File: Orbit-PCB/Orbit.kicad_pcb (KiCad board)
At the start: 2 copper layers, 149.8 x 115.2 mm, 129 parts, among them J1 PJ-3200B-4A, J2 AVR-ISP-6, Q1 2N7002, SW1 SW_Push, U1 ATmega32U4-MU, U2 PRTR5V0U2X, Y1 16MHz

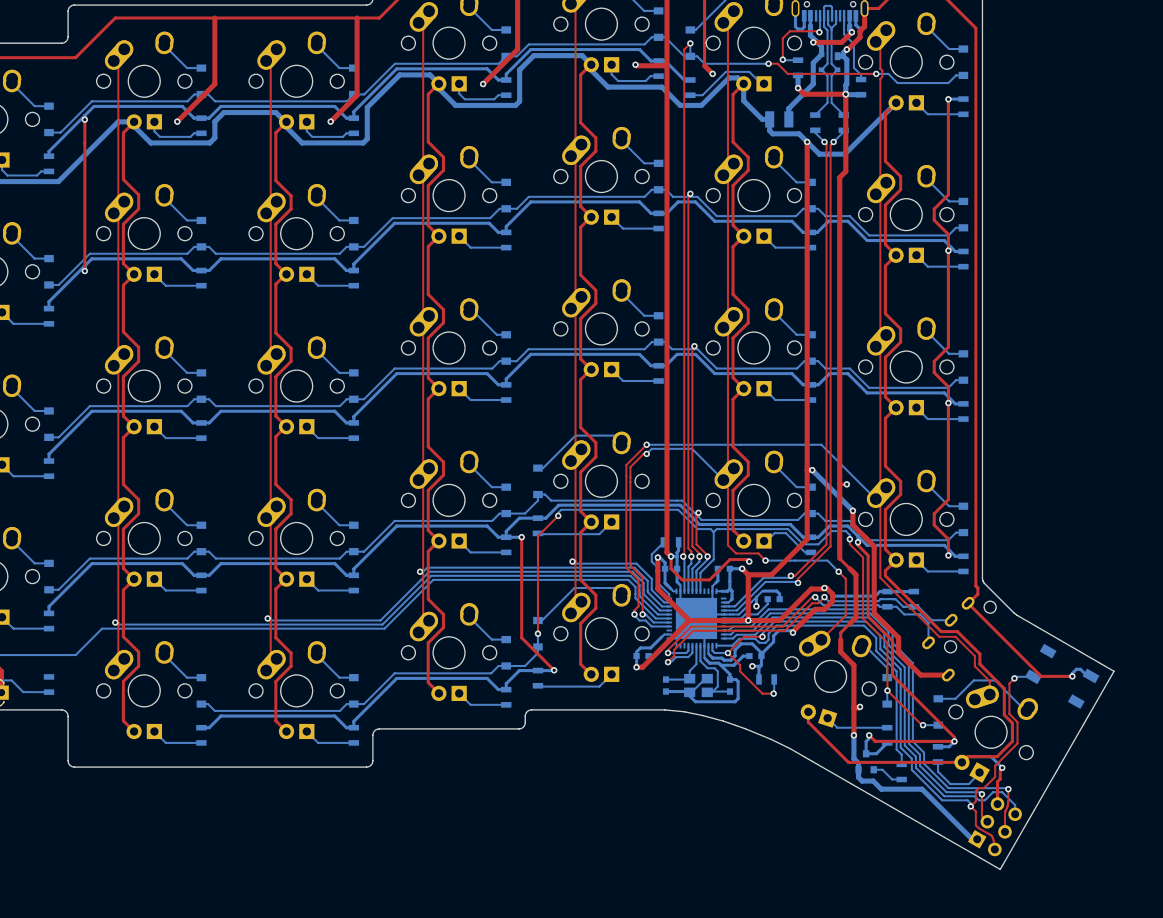
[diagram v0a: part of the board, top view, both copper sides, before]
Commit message: Round corner and route indicator LED
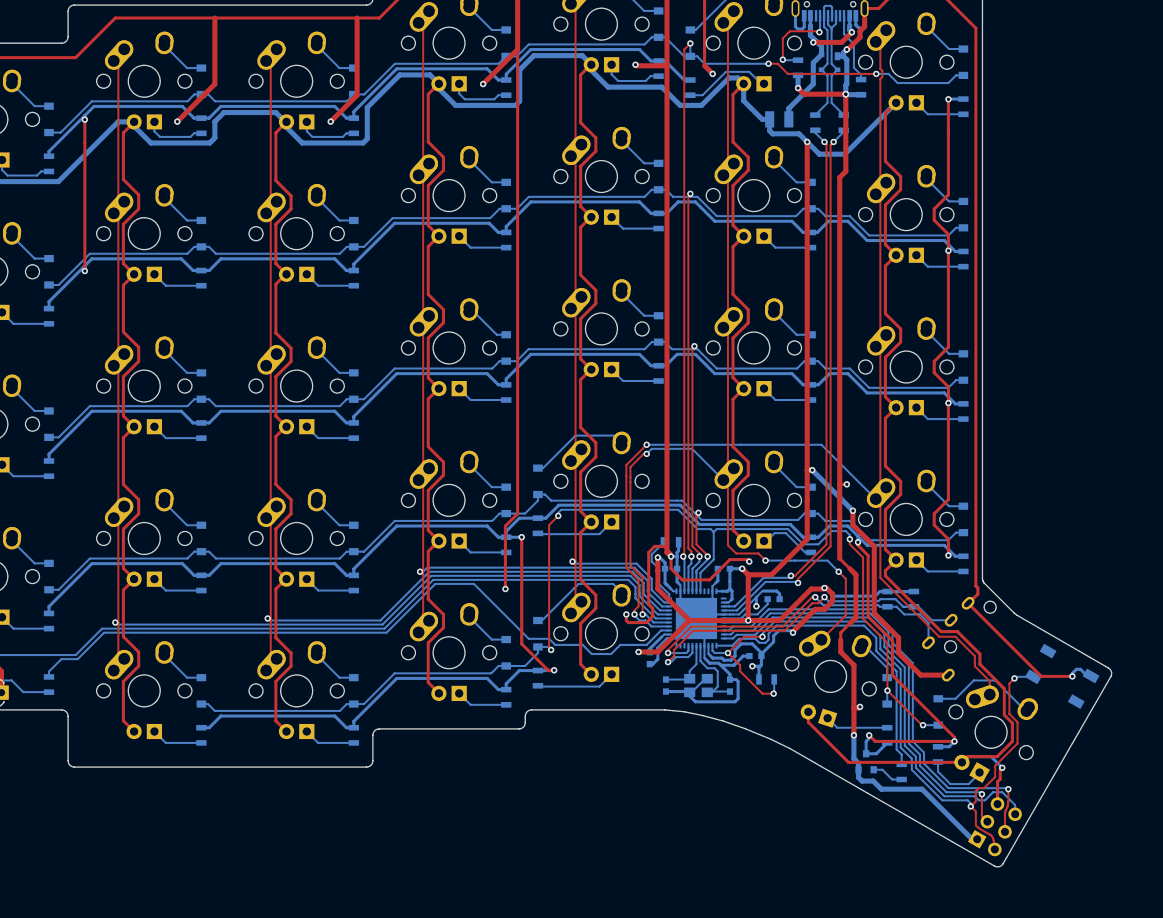
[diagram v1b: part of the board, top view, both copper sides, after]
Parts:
- moved C5 0.92 mm to (121.9, 117.3), turned to 270 degrees
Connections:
- U1 pad 25: Net-(U1-Pad25) -> LEDIND
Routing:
- net LEDIND: track 0.00 -> 87.6 mm
- net GND: track 678.0 -> 763.5 mm, vias 16 -> 18
- net +5V: track 969.3 -> 966.4 mm
- net ROW4: track 143.1 -> 144.8 mm
- net Net-(D32-Pad2): track 12.4 -> 13.4 mm
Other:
- board size 149.8 x 115.2 mm -> 149.5 x 114.9 mm
- net class POWER: trace_width 0.635 -> 0.381

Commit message: Both halves roughly complete, begin cleaning
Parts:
- added C10: 1uF, Capacitors_SMD:C_0603, B.Cu at (228.2, 116.1)
- added C11: 0.1uF, Capacitors_SMD:C_0603, B.Cu at (238.5, 122.5)
- added C12: 0.1uF, Capacitors_SMD:C_0603, B.Cu at (228.5, 110.6)
- added C13: 0.1uF, Capacitors_SMD:C_0603, B.Cu at (241.7, 112.1)
- added C14: 10uF, Capacitors_SMD:C_0603, B.Cu at (230.1, 120.7)
- added C8: 22pF, Capacitors_SMD:C_0603, B.Cu at (238.8, 108.0)
- added C9: 22pF, Capacitors_SMD:C_0603, B.Cu at (231.9, 108.0)
- added D36: SOD-123, Diodes_SMD:D_SOD-123, B.Cu at (204.0, 42.9)
- added D37: SOD-123, Diodes_SMD:D_SOD-123, B.Cu at (237.3, 40.5)
- added D38: SOD-123, Diodes_SMD:D_SOD-123, B.Cu at (256.4, 38.1)
- added D39: SOD-123, Diodes_SMD:D_SOD-123, B.Cu at (275.4, 40.5)
- added D40: SOD-123, Diodes_SMD:D_SOD-123, B.Cu at (294.5, 45.2)
- added D41: SOD-123, Diodes_SMD:D_SOD-123, B.Cu at (313.5, 45.2)
- added D42: SOD-123, Diodes_SMD:D_SOD-123, B.Cu at (332.6, 50.0)
- added D43: SOD-123, Diodes_SMD:D_SOD-123, B.Cu at (218.3, 61.9)
- added D44: SOD-123, Diodes_SMD:D_SOD-123, B.Cu at (237.3, 59.5)
- added D45: SOD-123, Diodes_SMD:D_SOD-123, B.Cu at (256.4, 57.1)
- added D46: SOD-123, Diodes_SMD:D_SOD-123, B.Cu at (275.4, 59.5)
- added D47: SOD-123, Diodes_SMD:D_SOD-123, B.Cu at (294.5, 64.3)
- added D48: SOD-123, Diodes_SMD:D_SOD-123, B.Cu at (313.5, 64.3)
- added D49: SOD-123, Diodes_SMD:D_SOD-123, B.Cu at (332.6, 69.1)
- added D50: SOD-123, Diodes_SMD:D_SOD-123, B.Cu at (218.3, 81.0)
- added D51: SOD-123, Diodes_SMD:D_SOD-123, B.Cu at (237.3, 78.6)
- added D52: SOD-123, Diodes_SMD:D_SOD-123, B.Cu at (256.4, 76.2)
- added D53: SOD-123, Diodes_SMD:D_SOD-123, B.Cu at (275.4, 78.6)
- added D54: SOD-123, Diodes_SMD:D_SOD-123, B.Cu at (294.5, 83.3)
- added D55: SOD-123, Diodes_SMD:D_SOD-123, B.Cu at (313.5, 83.3)
- added D56: SOD-123, Diodes_SMD:D_SOD-123, B.Cu at (332.6, 88.1)
- added D57: SOD-123, Diodes_SMD:D_SOD-123, B.Cu at (218.3, 100.0)
- added D58: SOD-123, Diodes_SMD:D_SOD-123, B.Cu at (237.5, 97.6)
- added D59: SOD-123, Diodes_SMD:D_SOD-123, B.Cu at (256.4, 95.2)
- added D60: SOD-123, Diodes_SMD:D_SOD-123, B.Cu at (275.4, 97.6)
- added D61: SOD-123, Diodes_SMD:D_SOD-123, B.Cu at (294.5, 102.4)
- added D62: SOD-123, Diodes_SMD:D_SOD-123, B.Cu at (313.5, 102.4)
- added D63: SOD-123, Diodes_SMD:D_SOD-123, B.Cu at (332.6, 107.2)
- added D64: SOD-123, Diodes_SMD:D_SOD-123, B.Cu at (207.1, 124.1)
- added D65: SOD-123, Diodes_SMD:D_SOD-123, B.Cu at (213.5, 124.1)
- added D66: SOD-123, Diodes_SMD:D_SOD-123, B.Cu at (256.4, 114.3)
- added D67: SOD-123, Diodes_SMD:D_SOD-123, B.Cu at (275.4, 116.7)
- added D68: SOD-123, Diodes_SMD:D_SOD-123, B.Cu at (294.5, 121.4)
- added D69: SOD-123, Diodes_SMD:D_SOD-123, B.Cu at (313.5, 121.4)
- added D70: LED_1.8mm, LEDs:LED_D3.0mm, F.Cu at (326.6, 122.2)
- added F2: 500mA, Fuse_Holders_and_Fuses:Fuse_SMD1206_Reflow, B.Cu at (217.5, 49.2)
- added J10: Breakaway_Tabs, locallib:breakaway-mousebites, F.Cu at (173.0, 100.0)
- added J11: PJ-3200B-4A, locallib:PJ-3200B-4A, B.Cu at (199.5, 109.9)
- added J12: AVR-ISP-6, Molex-0548190589:Reset_Pretty-Mask, B.Cu at (200.0, 138.4)
- added J13: Breakaway_Tabs, locallib:breakaway-mousebites, F.Cu at (201.6, 42.9)
- added J14: Breakaway_Tabs, locallib:breakaway-mousebites, F.Cu at (192.1, 42.9)
- added J15: Breakaway_Tabs, locallib:breakaway-mousebites, F.Cu at (201.6, 61.9)
- added J16: Breakaway_Tabs, locallib:breakaway-mousebites, F.Cu at (192.1, 61.9)
- added J17: Breakaway_Tabs, locallib:breakaway-mousebites, F.Cu at (201.6, 81.0)
- added J18: Breakaway_Tabs, locallib:breakaway-mousebites, F.Cu at (192.1, 81.0)
- added J19: Breakaway_Tabs, locallib:breakaway-mousebites, F.Cu at (201.6, 100.0)
- added J20: Breakaway_Tabs, locallib:breakaway-mousebites, F.Cu at (192.1, 100.0)
- added J3: Breakaway_Tabs, locallib:breakaway-mousebites, F.Cu at (163.5, 42.9)
- added J4: Breakaway_Tabs, locallib:breakaway-mousebites, F.Cu at (163.5, 61.9)
- added J5: Breakaway_Tabs, locallib:breakaway-mousebites, F.Cu at (163.5, 81.0)
- added J6: Breakaway_Tabs, locallib:breakaway-mousebites, F.Cu at (163.8, 100.0)
- added J7: Breakaway_Tabs, locallib:breakaway-mousebites, F.Cu at (173.0, 42.9)
- added J8: Breakaway_Tabs, locallib:breakaway-mousebites, F.Cu at (173.0, 61.9)
- added J9: Breakaway_Tabs, locallib:breakaway-mousebites, F.Cu at (173.0, 81.0)
- added MX35: MX-1U, MX_Alps_Hybrid:MX-1U, F.Cu at (211.1, 42.9)
- added MX36: MX-1U, MX_Alps_Hybrid:MX-1U, F.Cu at (230.2, 40.5)
- added MX37: MX-1U, MX_Alps_Hybrid:MX-1U, F.Cu at (249.2, 38.1)
- added MX38: MX-1U, MX_Alps_Hybrid:MX-1U, F.Cu at (268.3, 40.5)
- added MX39: MX-1U, MX_Alps_Hybrid:MX-1U, F.Cu at (287.3, 45.2)
- added MX40: MX-1U, MX_Alps_Hybrid:MX-1U, F.Cu at (306.4, 45.2)
- added MX41: MX-1U, MX_Alps_Hybrid:MX-1U, F.Cu at (325.4, 50.0)
- added MX42: MX-1U, MX_Alps_Hybrid:MX-1U, F.Cu at (211.1, 61.9)
- added MX43: MX-1U, MX_Alps_Hybrid:MX-1U, F.Cu at (230.2, 59.5)
- added MX44: MX-1U, MX_Alps_Hybrid:MX-1U, F.Cu at (249.2, 57.1)
- added MX45: MX-1U, MX_Alps_Hybrid:MX-1U, F.Cu at (268.3, 59.5)
- added MX46: MX-1U, MX_Alps_Hybrid:MX-1U, F.Cu at (287.3, 64.3)
- added MX47: MX-1U, MX_Alps_Hybrid:MX-1U, F.Cu at (306.4, 64.3)
- added MX48: MX-1U, MX_Alps_Hybrid:MX-1U, F.Cu at (325.4, 69.1)
- added MX49: MX-1U, MX_Alps_Hybrid:MX-1U, F.Cu at (211.1, 81.0)
- added MX50: MX-1U, MX_Alps_Hybrid:MX-1U, F.Cu at (230.2, 78.6)
- added MX51: MX-1U, MX_Alps_Hybrid:MX-1U, F.Cu at (249.2, 76.2)
- added MX52: MX-1U, MX_Alps_Hybrid:MX-1U, F.Cu at (268.3, 78.6)
- added MX53: MX-1U, MX_Alps_Hybrid:MX-1U, F.Cu at (287.3, 83.3)
- added MX54: MX-1U, MX_Alps_Hybrid:MX-1U, F.Cu at (306.4, 83.3)
- added MX55: MX-1U, MX_Alps_Hybrid:MX-1U, F.Cu at (325.4, 88.1)
- added MX56: MX-1U, MX_Alps_Hybrid:MX-1U, F.Cu at (211.1, 100.0)
- added MX57: MX-1U, MX_Alps_Hybrid:MX-1U, F.Cu at (230.2, 97.6)
- added MX58: MX-1U, MX_Alps_Hybrid:MX-1U, F.Cu at (249.2, 95.2)
- added MX59: MX-1U, MX_Alps_Hybrid:MX-1U, F.Cu at (268.3, 97.6)
- added MX60: MX-1U, MX_Alps_Hybrid:MX-1U, F.Cu at (287.3, 102.4)
- added MX61: MX-1U, MX_Alps_Hybrid:MX-1U, F.Cu at (306.4, 102.4)
- added MX62: MX-1U, MX_Alps_Hybrid:MX-1U, F.Cu at (325.4, 107.2)
- added MX63: MX-1.5U, MX_Alps_Hybrid:MX-1.5U-Vertical, F.Cu at (200.5, 126.6)
- added MX64: MX-1U, MX_Alps_Hybrid:MX-1U, F.Cu at (220.6, 119.6)
- added MX65: MX-1U, MX_Alps_Hybrid:MX-1U, F.Cu at (249.2, 114.3)
- added MX66: MX-1U, MX_Alps_Hybrid:MX-1U, F.Cu at (268.3, 116.7)
- added MX67: MX-1U, MX_Alps_Hybrid:MX-1U, F.Cu at (287.3, 121.4)
- added MX68: MX-1U, MX_Alps_Hybrid:MX-1U, F.Cu at (306.4, 121.4)
- added Q2: 2N7002, TO_SOT_Packages_SMD:SOT-23, B.Cu at (209.6, 110.1)
- added R45: 10k, Resistors_SMD:R_0805, B.Cu at (225.8, 110.6)
- added R46: 470, Resistors_SMD:R_0805, B.Cu at (204.0, 48.4)
- added R47: 470, Resistors_SMD:R_0805, B.Cu at (237.3, 46.0)
- added R48: 470, Resistors_SMD:R_0805, B.Cu at (256.4, 43.7)
- added R49: 470, Resistors_SMD:R_0805, B.Cu at (275.4, 46.0)
- added R50: 470, Resistors_SMD:R_0805, B.Cu at (294.5, 50.8)
- added R51: 470, Resistors_SMD:R_0805, B.Cu at (313.5, 50.8)
- added R52: 470, Resistors_SMD:R_0805, B.Cu at (332.6, 55.6)
- added R53: 470, Resistors_SMD:R_0805, B.Cu at (218.3, 67.5)
- added R54: 470, Resistors_SMD:R_0805, B.Cu at (237.3, 65.1)
- added R55: 470, Resistors_SMD:R_0805, B.Cu at (256.4, 62.7)
- added R56: 470, Resistors_SMD:R_0805, B.Cu at (275.4, 65.1)
- added R57: 470, Resistors_SMD:R_0805, B.Cu at (294.5, 69.8)
- added R58: 470, Resistors_SMD:R_0805, B.Cu at (313.5, 69.8)
- added R59: 470, Resistors_SMD:R_0805, B.Cu at (332.6, 74.6)
- added R60: 470, Resistors_SMD:R_0805, B.Cu at (218.3, 86.5)
- added R61: 470, Resistors_SMD:R_0805, B.Cu at (237.3, 84.1)
- added R62: 470, Resistors_SMD:R_0805, B.Cu at (256.4, 81.8)
- added R63: 470, Resistors_SMD:R_0805, B.Cu at (275.4, 84.1)
- added R64: 470, Resistors_SMD:R_0805, B.Cu at (294.5, 88.9)
- added R65: 470, Resistors_SMD:R_0805, B.Cu at (313.5, 88.9)
- added R66: 470, Resistors_SMD:R_0805, B.Cu at (332.6, 93.7)
- added R67: 10k, Resistors_SMD:R_0805, B.Cu at (242.2, 121.5)
- added R68: 470, Resistors_SMD:R_0805, B.Cu at (218.3, 105.6)
- added R69: 470, Resistors_SMD:R_0805, B.Cu at (237.5, 103.2)
- added R70: 470, Resistors_SMD:R_0805, B.Cu at (256.4, 100.8)
- added R71: 470, Resistors_SMD:R_0805, B.Cu at (275.4, 103.2)
- added R72: 470, Resistors_SMD:R_0805, B.Cu at (294.5, 108.0)
- added R73: 470, Resistors_SMD:R_0805, B.Cu at (313.5, 108.0)
- added R74: 470, Resistors_SMD:R_0805, B.Cu at (332.6, 112.7)
- added R75: 470, Resistors_SMD:R_0805, B.Cu at (208.8, 129.4)
- added R76: 470, Resistors_SMD:R_0805, B.Cu at (213.5, 129.4)
- added R77: 470, Resistors_SMD:R_0805, B.Cu at (256.4, 119.9)
- added R78: 470, Resistors_SMD:R_0805, B.Cu at (275.4, 122.2)
- added R79: 470, Resistors_SMD:R_0805, B.Cu at (294.5, 127.0)
- added R80: 470, Resistors_SMD:R_0805, B.Cu at (313.5, 127.0)
- added R81: 1k, Resistors_SMD:R_0805, B.Cu at (213.6, 110.1)
- added R82: 1k, Resistors_SMD:R_0805, B.Cu at (319.1, 120.7)
- added R83: 22, Resistors_SMD:R_0805, B.Cu at (222.2, 43.7)
- added R84: 22, Resistors_SMD:R_0805, B.Cu at (219.1, 43.7)
- added R85: 5.1k, Resistors_SMD:R_0805, B.Cu at (228.6, 32.5)
- added R86: 5.1k, Resistors_SMD:R_0805, B.Cu at (209.6, 34.9)
- added SW2: SW_Push, Molex-0548190589:SKQG-1155865, B.Cu at (192.1, 119.8)
- added U3: ATmega32U4-MU, Housings_DFN_QFN:QFN-44-1EP_7x7mm_Pitch0.5mm, B.Cu at (235.5, 116.0)
- added U4: PRTR5V0U2X, locallib:SOT143B, B.Cu at (220.7, 38.9)
- added USB2: HRO-TYPE-C-31-M-12, Type-C:HRO-TYPE-C-31-M-12-Assembly, B.Cu at (220.7, 27.0)
- added Y2: 16MHz, Crystals:Crystal_SMD_2520-4pin_2.5x2.0mm, B.Cu at (235.3, 108.0)
- Y1: footprint Crystals:Crystal_SMD_3225-4pin_3.2x2.5mm -> Crystals:Crystal_SMD_2520-4pin_2.5x2.0mm
- moved R44 13.1 mm to (133.3, 32.5), turned to 180 degrees
- moved R43 11.8 mm to (152.4, 34.9), turned to 0 degrees
- moved R42 6.77 mm to (142.9, 43.7)
- moved R41 6.76 mm to (146.1, 43.7)
- moved U2 3.97 mm to (144.4, 38.9)
- moved F1 3.27 mm to (141.3, 49.2), turned to 90 degrees
- moved USB1 2.38 mm to (144.5, 27.0)
- moved C5 1.02 mm to (120.9, 117.5)
- moved C1 0.68 mm to (124.6, 120.5)
- moved C2 0.57 mm to (131.4, 120.5)
- moved Y1 0.25 mm to (128.0, 120.5)
- turned SW1 to 150 degrees
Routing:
- net +5VA: track 0.00 -> 967.3 mm, vias 0 -> 9
- net GNDA: track 0.00 -> 744.8 mm, vias 0 -> 20
- net LEDGND-R: track 0.00 -> 711.3 mm, vias 0 -> 12
- net ROW0-R: track 0.00 -> 239.3 mm, vias 0 -> 3
- net ROW4-R: track 0.00 -> 224.1 mm, vias 0 -> 6
- net ROW1-R: track 0.00 -> 206.6 mm, vias 0 -> 2
- net ROW2-R: track 0.00 -> 185.4 mm, vias 0 -> 2
- net ROW3-R: track 0.00 -> 164.9 mm, vias 0 -> 2
- net COL6-R: track 0.00 -> 154.6 mm, vias 0 -> 1
- net COL5-R: track 0.00 -> 153.2 mm
- net COL0-R: track 0.00 -> 153.0 mm, vias 0 -> 1
- net COL1-R: track 0.00 -> 143.0 mm, vias 0 -> 4
- net COL4-R: track 0.00 -> 133.6 mm, vias 0 -> 1
- net COL3-R: track 0.00 -> 112.4 mm
- net LEDIND-R: track 0.00 -> 92.5 mm
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- added copper zone on B.Cu, net GNDA
- added copper zone on F.Cu, net GNDA
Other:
- board size 149.5 x 114.9 mm -> 304.8 x 114.9 mm

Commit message: Reroute some traces
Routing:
- net GND: track 781.4 -> 1077.7 mm, vias 17 -> 20
- net GNDA: track 744.8 -> 803.3 mm, vias 20 -> 26
- net +5V: track 958.9 -> 1001.8 mm, vias 10 -> 9
- net RESET: track 70.3 -> 100.1 mm, vias 4 -> 5
- net ROW4-R: track 224.1 -> 236.8 mm
- net COL1-R: track 143.0 -> 136.9 mm
- net SDA: track 44.0 -> 48.1 mm
- net SCL: track 44.3 -> 45.9 mm
- net Net-(D64-Pad2): track 7.09 -> 8.54 mm
- net MOSI: track 54.0 -> 52.7 mm
- net +5VA: track 967.3 -> 966.4 mm
- net SDA-R: track 45.7 -> 44.9 mm
- net Net-(MX51-Pad4): track 6.46 -> 7.31 mm
- net SCL-R: track 48.5 -> 47.7 mm
- net Net-(MX50-Pad4): track 6.46 -> 7.28 mm
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- added copper zone on B.Cu, net (none)
- added copper zone on F.Cu, net (none)

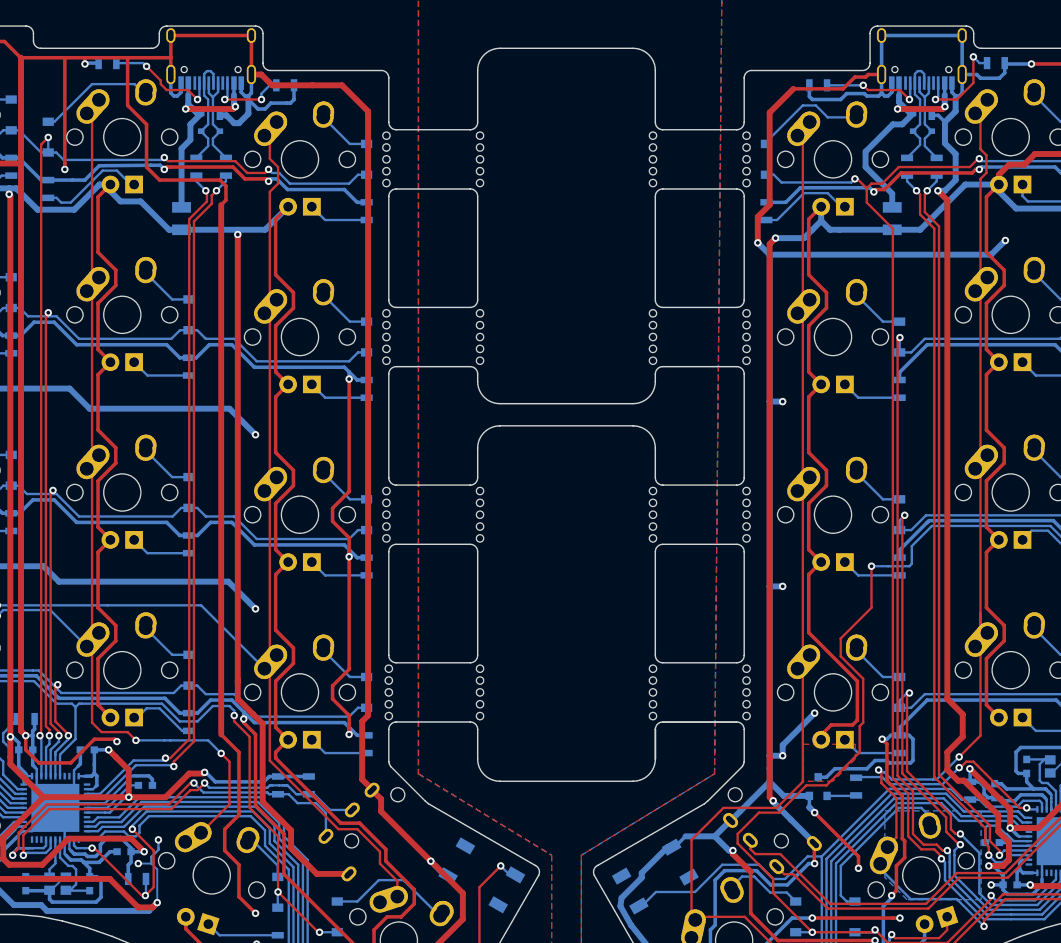
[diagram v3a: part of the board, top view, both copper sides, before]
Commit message: Repair DRC errors
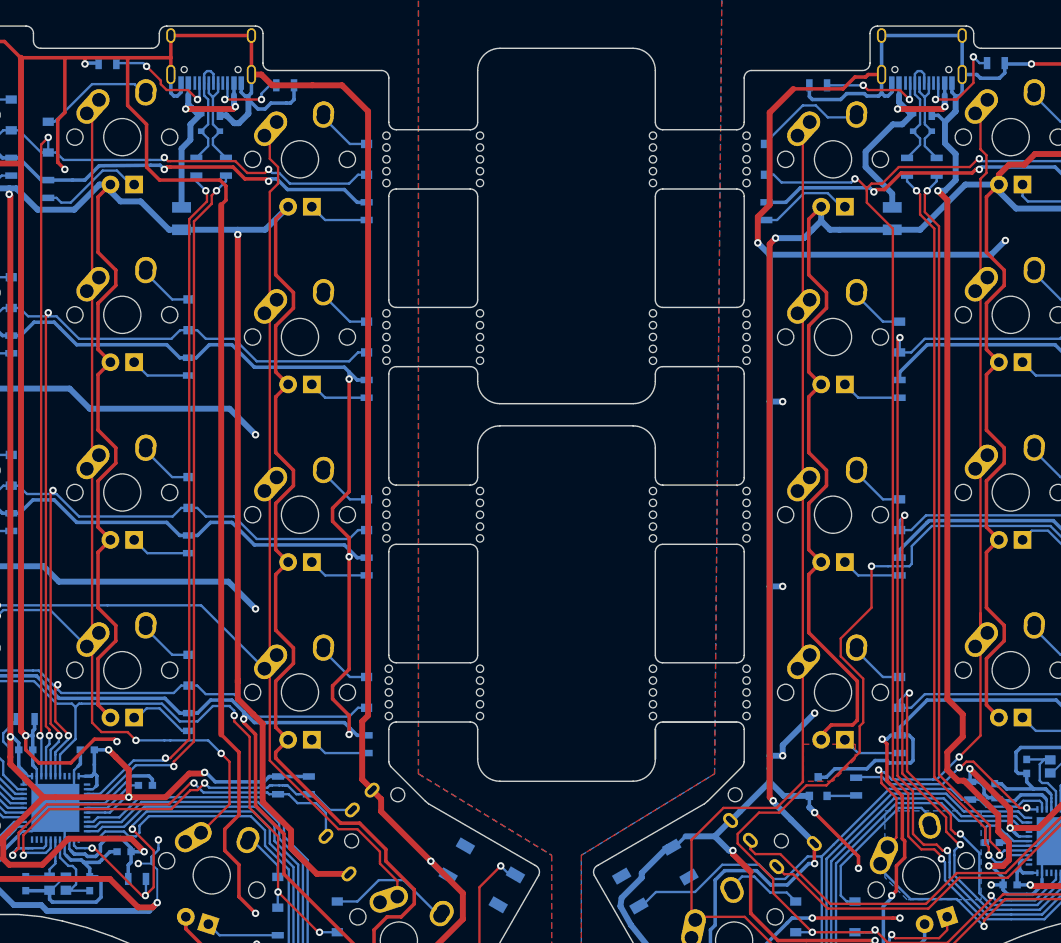
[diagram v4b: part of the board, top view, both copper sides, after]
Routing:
- net GND: track 1077.7 -> 1078.4 mm
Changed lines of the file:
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@@
     (thickness 1.6)
     (drawings 204)
-    (tracks 3549)
+    (tracks 3551)
     (zones 0)
     (modules 272)
@@
   (segment (start 131.953 105.029) (end 134.112 105.029) (width 0.381) (layer F.Cu) (net 1))
   (segment (start 134.112 105.029) (end 134.366 105.283) (width 0.381) (layer F.Cu) (net 1))
-  (segment (start 128.778 43.307) (end 128.778 31.96875) (width 0.381) (layer F.Cu) (net 1))
   (segment (start 128.778 31.96875) (end 124.04375 31.96875) (width 0.381) (layer F.Cu) (net 1))
   (segment (start 40.894 118.999) (end 38.354 116.459) (width 0.635) (layer F.Cu) (net 1))
@@
   (segment (start 138.049 118.364) (end 136.652 118.364) (width 0.2032) (layer B.Cu) (net 1))
   (via (at 128.778 43.942) (size 0.8) (drill 0.4) (layers F.Cu B.Cu) (net 1))
-  (segment (start 128.778 43.307) (end 128.778 43.942) (width 0.381) (layer F.Cu) (net 1))
   (segment (start 169.872321 119.686147) (end 169.597147 119.686147) (width 0.635) (layer B.Cu) (net 1))
   (via (at 168.021 118.11) (size 0.8) (drill 0.4) (layers F.Cu B.Cu) (net 1))
@@
   (segment (start 160.401 134.366) (end 160.782 133.985) (width 0.635) (layer F.Cu) (net 1))
   (segment (start 160.02 134.747) (end 160.401 134.366) (width 0.635) (layer F.Cu) (net 1))
+  (segment (start 128.016 43.18) (end 128.778 43.942) (width 0.381) (layer F.Cu) (net 1))
+  (segment (start 128.016 38.608) (end 128.016 43.18) (width 0.381) (layer F.Cu) (net 1))
+  (segment (start 128.778 31.96875) (end 128.778 37.846) (width 0.381) (layer F.Cu) (net 1))
+  (segment (start 128.778 37.846) (end 128.016 38.608) (width 0.381) (layer F.Cu) (net 1))
   (segment (start 127.762 115.795) (end 127.762 118.11) (width 0.254) (layer B.Cu) (net 2))
   (segment (start 127.141 119.823) (end 127.141 118.985) (width 0.254) (layer B.Cu) (net 2))
@@
   (segment (start 223.139 41.148) (end 223.139 38.862) (width 0.635) (layer B.Cu) (net 116))
   (segment (start 223.139 38.862) (end 222.42075 38.14375) (width 0.381) (layer B.Cu) (net 116))
-  (segment (start 229.374 120.65) (end 229.374 119.646) (width 0.381) (layer B.Cu) (net 116))
   (via (at 209.169 112.903) (size 0.8) (drill 0.4) (layers F.Cu B.Cu) (net 116))
   (segment (start 208.6 112.329) (end 208.6 112.334) (width 0.635) (layer B.Cu) (net 116))
@@
   (segment (start 229.362 118.618) (end 227.838 118.618) (width 0.635) (layer F.Cu) (net 116))
   (segment (start 229.997 117.983) (end 229.362 118.618) (width 0.635) (layer F.Cu) (net 116))
-  (segment (start 228.346 118.618) (end 229.374 119.646) (width 0.381) (layer B.Cu) (net 116))
-  (segment (start 227.838 118.618) (end 228.346 118.618) (width 0.381) (layer B.Cu) (net 116))
   (via (at 228.092 120.65) (size 0.8) (drill 0.4) (layers F.Cu B.Cu) (net 116))
   (segment (start 229.374 120.65) (end 228.092 120.65) (width 0.381) (layer B.Cu) (net 116))
@@
   (segment (start 256.286 85.217) (end 256.286 82.042) (width 0.635) (layer F.Cu) (net 116))
   (segment (start 259.715 32.766) (end 259.715 78.613) (width 0.635) (layer F.Cu) (net 116))
+  (segment (start 228.104 118.618) (end 229.374 119.888) (width 0.381) (layer B.Cu) (net 116))
+  (segment (start 227.838 118.618) (end 228.104 118.618) (width 0.381) (layer B.Cu) (net 116))
+  (segment (start 229.374 120.65) (end 229.374 119.888) (width 0.381) (layer B.Cu) (net 116))
   (segment (start 234.09925 107.2) (end 234.19925 107.1) (width 0.254) (layer B.Cu) (net 117))
   (segment (start 234.37425 107.2) (end 234.42425 107.25) (width 0.254) (layer B.Cu) (net 117))
